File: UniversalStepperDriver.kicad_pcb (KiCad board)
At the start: 2 copper layers, 65 x 56.5 mm, 84 parts, among them P1 USB_OTG, P11 CONN_01X04, P12 CONN_01X02, P13 CONN_28BYJ-48, P14 CONN_28BYJ-48, P15 CONN_28BYJ-48, P17 CONN_01X04, P2 CONN_01X02, P3 CONN_01X02, P4 CONN_01X03, P5 Universal_Serial_Connector, P6 CONN_01X06, P7 RPI_header, P8 CONN_01X03, P9 CONN_01X04, SW1 SW_PUSH, SW2 SW_PUSH, SW3 SW_PUSH, U1 STM32F411RE, U2 INA169, U3 MPQ4420, U4 ULN2003V, U5 ULN2003V, Y1 CRYSTAL_SMD

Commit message: all connected
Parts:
- JP1: moved to B.Cu
- SW1: footprint Buttons_Switches_SMD:SW_SPST_SKQG -> KSEK43J_LFS_TACTILE_SWITCH:KSEK43J_LFS_TACTILE_SWITCH
- SW2, SW3: footprint Buttons_Switches_SMD:SW_SPST_EVQP7C -> Buttons_Switches_ThroughHole:SW_Tactile_SPST_Angled
- Y1: value CRYSTAL_SMD -> CRYSTAL_SMD_16MHz
- moved JP1 28.3 mm to (113.7, 87.8), turned to 0 degrees
- moved R12 8.06 mm to (125.3, 111.4)
- moved D2 8.06 mm to (123.4, 111.3)
- moved R27 7.57 mm to (106.4, 109.2), turned to 180 degrees
- moved C16 7.44 mm to (113.5, 107.4)
- moved R16 6.22 mm to (115.0, 115.9), turned to 90 degrees
- moved R10 5.67 mm to (118.5, 120.2), turned to 0 degrees
- moved C13 5.64 mm to (112.3, 114.7)
- moved D1 4.74 mm to (129.8, 111.4)
- moved R11 4.65 mm to (131.7, 111.4)
- moved R25 4.38 mm to (109.7, 109.2), turned to 180 degrees
- moved P9 3.92 mm to (114.0, 97.1)
- moved JP6 3.62 mm to (109.8, 81.1), turned to 180 degrees
- moved P11 3.61 mm to (110.4, 97.1)
- moved R15 3.57 mm to (112.5, 120.0), turned to 270 degrees
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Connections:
- C12 pad 1: /X_MAX -> /X_LIMIT
- C13 pad 1: /Y_MAX -> /Y_LIMIT
- R13 pad 2: /X_MAX -> /X_LIMIT
- R14 pad 2: /Y_MAX -> /Y_LIMIT
- SW2 pad 1: /X_MAX -> /X_LIMIT
- SW3 pad 1: /Y_MAX -> /Y_LIMIT
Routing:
- net GND: track 46.8 -> 452.0 mm, vias 5 -> 23
- net +3V3: track 10.3 -> 235.6 mm, vias 0 -> 14
- net /X_LIMIT: track 23.1 -> 73.6 mm, vias 0 -> 1
- net /SDA_I2C: track 0.00 -> 44.8 mm, vias 0 -> 1
- net /RxD: track 24.6 -> 65.4 mm, vias 1 -> 4
- net /SCL_I2C: track 0.00 -> 40.6 mm, vias 0 -> 1
- net /Y_LIMIT: track 31.2 -> 68.8 mm
- net /RST: track 7.25 -> 43.5 mm, vias 0 -> 2
- net /GPI: track 0.00 -> 35.1 mm
- net /SERVO_PWM: track 0.00 -> 33.7 mm, vias 0 -> 1
- net /SCK_SPI: track 0.00 -> 32.5 mm, vias 0 -> 1
- net /Y_ENC_A: track 0.00 -> 31.4 mm, vias 0 -> 1
- net /X_ENC_B: track 0.00 -> 29.6 mm, vias 0 -> 1
- net /Y_ENC_B: track 0.00 -> 27.8 mm, vias 0 -> 1
- net /X_ENC_A: track 0.00 -> 25.7 mm, vias 0 -> 1
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
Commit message: rev0.1 board done
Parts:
- added G***: LOGO, .pretty:LOGO_irnas1, B.Cu at (138.0, 100.2)
- moved P8 0.98 mm to (148.7, 111.1)
- moved C2 0.60 mm to (118.2, 101.4)
- moved C4 0.60 mm to (119.7, 101.4)
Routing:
- net +3V3: track 235.6 -> 278.9 mm
- net VAA: track 107.7 -> 117.4 mm
- net VCC: track 30.9 -> 34.9 mm
- net /USB_D_N: track 43.3 -> 44.5 mm
- net /STPEN: track 29.7 -> 28.9 mm
- net /SERVO_PWM: track 33.7 -> 32.9 mm
- net /M1_STEP: track 31.3 -> 30.8 mm
- net GND: track 452.0 -> 452.5 mm
- added copper zone on F.Cu, net +3V3
- added copper zone on B.Cu, net GND
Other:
- board text added: "+"
- board text added: "-"
- board text added: "CERN OHL"
- board text added: "F"
- board text added: "USB"
- board text added: "Universal Stepper Driver"
- board text added: "VCC"
- board text added: "V_3"
- board text added: "WWW.IRNAS.EU"
- board text added: "X"
- board text added: "Y"
- board text added: "s"
- board text removed: "CERN OHL V1.2"
- board text removed: "Julien M."

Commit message: add gerber and BOM
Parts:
- C10: footprint Capacitors_SMD:C_0603 -> Capacitors_SMD:C_1206
- moved C10 0.64 mm to (161.6, 74.2)
- turned JP7 to 90 degrees
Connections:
- Y1 pad 2: Net-(Y1-Pad2) -> GND
- Y1 pad 4: (no net) -> GND
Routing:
- net GND: track 452.5 -> 460.8 mm
- net 5V_RPi: track 54.9 -> 50.7 mm
- net VAA: track 117.4 -> 116.5 mm
- net /C_X_4: track 29.2 -> 29.8 mm

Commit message: P5 footprint fix
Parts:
- P5: footprint .pretty:micromatch -> micromatch
- moved JP3 3.80 mm to (116.1, 83.6)
- moved JP1 2.95 mm to (116.1, 86.1)
- moved JP6 1.06 mm to (108.8, 81.2)
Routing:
- net /MISO_SPI: track 36.6 -> 32.5 mm
- net /TxD: track 49.5 -> 46.9 mm
- net Net-(JP1-Pad1): track 5.66 -> 3.81 mm
- net /SCL_I2C: track 40.6 -> 39.0 mm
- net Net-(JP3-Pad1): track 5.44 -> 3.86 mm
- net /CS_SPI: track 24.3 -> 25.8 mm
- net Net-(JP5-Pad1): track 6.83 -> 7.97 mm
- net /RxD: track 65.4 -> 66.3 mm
- net /F_LIMIT: track 50.0 -> 50.7 mm
- net GND: track 460.8 -> 461.4 mm, vias 23 -> 22

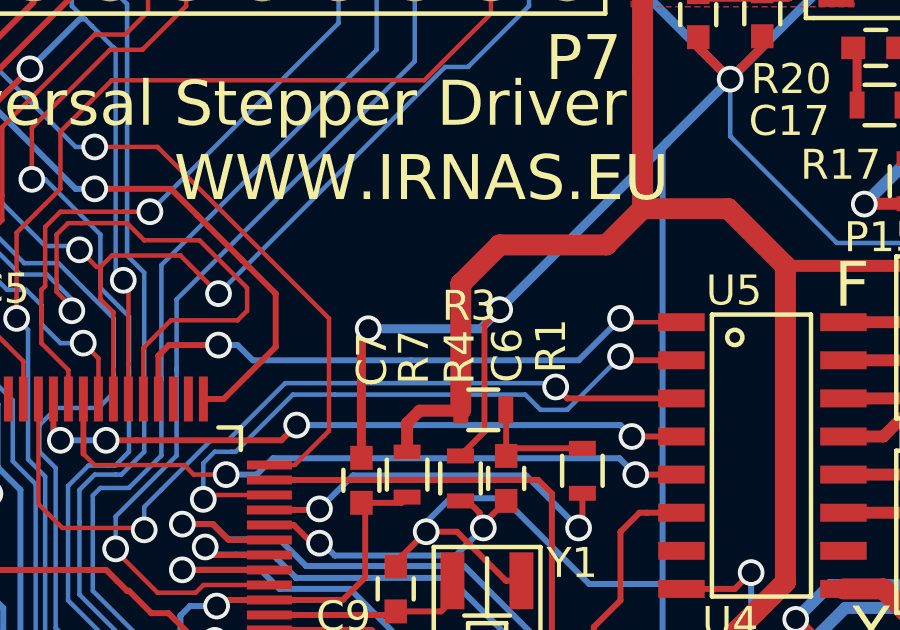
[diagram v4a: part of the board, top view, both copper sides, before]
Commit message: PWR LED add Fixes #3
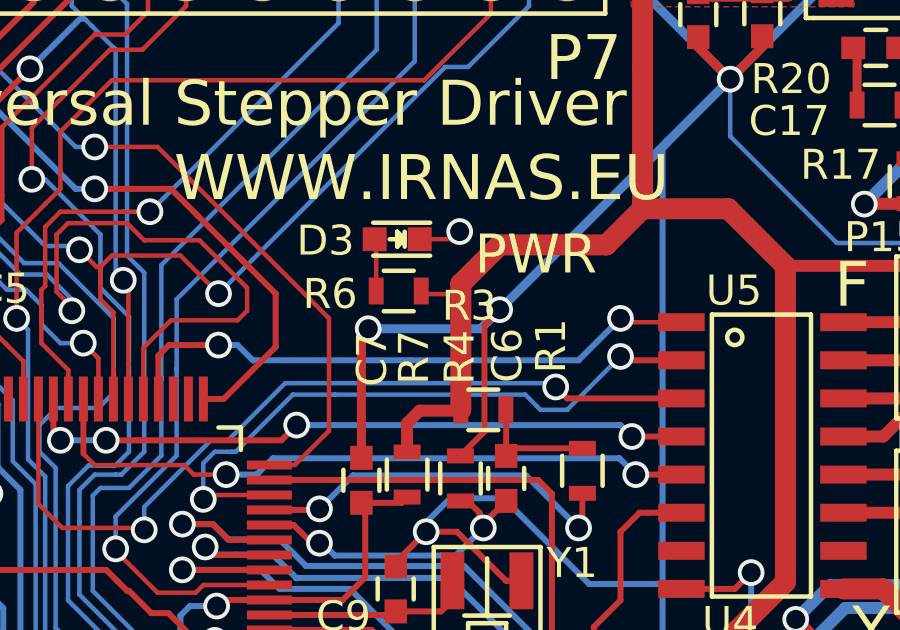
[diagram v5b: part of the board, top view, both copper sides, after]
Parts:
- added D3: LED_GREEN, LEDs:LED_0603, F.Cu at (138.1, 84.8)
- added R6: 1k, Resistors_SMD:R_0603, F.Cu at (138.2, 86.6)
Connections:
- Y1 pad 2: GND -> Net-(Y1-Pad2)
- Y1 pad 4: GND -> (no net)
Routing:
- net Net-(D3-Pad2): track 0.00 -> 1.75 mm
- net +3V3: track 278.9 -> 280.3 mm
- net GND: track 461.4 -> 462.4 mm, vias 22 -> 23
- net Net-(Y1-Pad2): track 0.00 -> 0.51 mm
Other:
- board text added: "PWR"
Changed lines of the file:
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@@
 (kicad_pcb (version 4) (host pcbnew 4.0.2-stable)
   (general
-    (links 224)
+    (links 225)
     (no_connects 0)
-    (area 100.838261 67.828761 177.679167 136.400001)
+    (area 104.869999 71.019999 169.970001 127.620001)
     (thickness 1.6)
-    (drawings 35)
-    (tracks 1645)
+    (drawings 36)
+    (tracks 1653)
     (zones 0)
-    (modules 85)
-    (nets 108)
+    (modules 87)
+    (nets 110)
   )
   (page A4)
@@
   (net 106 "Net-(U5-Pad10)")
   (net 107 "Net-(U1-Pad30)")
+  (net 108 "Net-(Y1-Pad2)")
+  (net 109 "Net-(D3-Pad2)")
   (net_class Default "This is the default net class."
     (clearance 0.15)
@@
     (add_net "Net-(D1-Pad2)")
     (add_net "Net-(D2-Pad2)")
+    (add_net "Net-(D3-Pad2)")
     (add_net "Net-(F1-Pad1)")
     (add_net "Net-(JP1-Pad1)")
@@
     (add_net "Net-(U5-Pad10)")
     (add_net "Net-(U5-Pad7)")
+    (add_net "Net-(Y1-Pad2)")
     (add_net VAA)
     (add_net VCC)
@@
       (net 9 /OSCIN_8M))
     (pad 2 smd rect (at 3.7 0 90) (size 1.9 0.8) (layers F.Cu F.Paste F.Mask)
-      (net 1 GND))
+      (net 108 "Net-(Y1-Pad2)"))
     (pad 3 smd rect (at 3.7 -2.3 90) (size 1.9 0.8) (layers F.Cu F.Paste F.Mask)
       (net 10 /OSCOUT_8M))
-    (pad 4 smd rect (at 0 -2.3 90) (size 1.9 0.8) (layers F.Cu F.Paste F.Mask)
-      (net 1 GND))
+    (pad 4 smd rect (at 0 -2.3 90) (size 1.9 0.8) (layers F.Cu F.Paste F.Mask))
   )
   (module .pretty:bridgeJumper (layer B.Cu)
@@
     )
   )
+  (module LEDs:LED_0603 (layer F.Cu)
+    (at 138.1252 84.836 180)
+    (descr "LED 0603 smd package")
+    (tags "LED led 0603 SMD smd SMT smt smdled SMDLED smtled SMTLED")
+    (attr smd)
+    (fp_text reference D3 (at 2.3876 -0.0508 180) (layer F.SilkS)
+      (effects (font (size 1 1) (thickness 0.15)))
+    )
+    (fp_text value LED_GREEN (at 0 1.5 180) (layer F.Fab)
+      (effects (font (size 1 1) (thickness 0.15)))
+    )
+    (fp_line (start -1.1 0.55) (end 0.8 0.55) (layer F.SilkS) (width 0.15))
+    (fp_line (start -1.1 -0.55) (end 0.8 -0.55) (layer F.SilkS) (width 0.15))
+    (fp_line (start -0.2 0) (end 0.25 0) (layer F.SilkS) (width 0.15))
+    (fp_line (start -0.25 -0.25) (end -0.25 0.25) (layer F.SilkS) (width 0.15))
+    (fp_line (start -0.25 0) (end 0 -0.25) (layer F.SilkS) (width 0.15))
+    (fp_line (start 0 -0.25) (end 0 0.25) (layer F.SilkS) (width 0.15))
+    (fp_line (start 0 0.25) (end -0.25 0) (layer F.SilkS) (width 0.15))
+    (fp_line (start 1.4 -0.75) (end 1.4 0.75) (layer F.CrtYd) (width 0.05))
+    (fp_line (start 1.4 0.75) (end -1.4 0.75) (layer F.CrtYd) (width 0.05))
+    (fp_line (start -1.4 0.75) (end -1.4 -0.75) (layer F.CrtYd) (width 0.05))
+    (fp_line (start -1.4 -0.75) (end 1.4 -0.75) (layer F.CrtYd) (width 0.05))
+    (pad 2 smd rect (at 0.7493 0) (size 0.79756 0.79756) (layers F.Cu F.Paste F.Mask)
+      (net 109 "Net-(D3-Pad2)"))
+    (pad 1 smd rect (at -0.7493 0) (size 0.79756 0.79756) (layers F.Cu F.Paste F.Mask)
+      (net 1 GND))
+    (model LEDs.3dshapes/LED_0603.wrl
+      (at (xyz 0 0 0))
+      (scale (xyz 1 1 1))
+      (rotate (xyz 0 0 180))
+    )
+  )
+  (module Resistors_SMD:R_0603 (layer F.Cu)
+    (at 138.176 86.5632)
+    (descr "Resistor SMD 0603, reflow soldering, Vishay (see dcrcw.pdf)")
+    (tags "resistor 0603")
+    (attr smd)
+    (fp_text reference R6 (at -2.286 0.1016) (layer F.SilkS)
+      (effects (font (size 1 1) (thickness 0.15)))
+    )
+    (fp_text value 1k (at 0 1.9) (layer F.Fab)
+      (effects (font (size 1 1) (thickness 0.15)))
+    )
+    (fp_line (start -1.3 -0.8) (end 1.3 -0.8) (layer F.CrtYd) (width 0.05))
+    (fp_line (start -1.3 0.8) (end 1.3 0.8) (layer F.CrtYd) (width 0.05))
+    (fp_line (start -1.3 -0.8) (end -1.3 0.8) (layer F.CrtYd) (width 0.05))
+    (fp_line (start 1.3 -0.8) (end 1.3 0.8) (layer F.CrtYd) (width 0.05))
+    (fp_line (start 0.5 0.675) (end -0.5 0.675) (layer F.SilkS) (width 0.15))
+    (fp_line (start -0.5 -0.675) (end 0.5 -0.675) (layer F.SilkS) (width 0.15))
+    (pad 1 smd rect (at -0.75 0) (size 0.5 0.9) (layers F.Cu F.Paste F.Mask)
+      (net 109 "Net-(D3-Pad2)"))
+    (pad 2 smd rect (at 0.75 0) (size 0.5 0.9) (layers F.Cu F.Paste F.Mask)
+      (net 2 +3V3))
+    (model Resistors_SMD.3dshapes/R_0603.wrl
+      (at (xyz 0 0 0))
+      (scale (xyz 1 1 1))
+      (rotate (xyz 0 0 0))
+    )
+  )
+  (gr_text PWR (at 142.748 85.344) (layer F.SilkS)
+    (effects (font (size 1.3 1.3) (thickness 0.3)))
+  )
   (gr_text V_3 (at 121.412 82.7405) (layer F.SilkS)
     (effects (font (size 1.5 1.5) (thickness 0.3)))
@@
   (gr_arc (start 166.92 74.07) (end 166.92 71.07) (angle 90) (layer Edge.Cuts) (width 0.1))
   (gr_arc (start 107.92 124.57) (end 107.92 127.57) (angle 90) (layer Edge.Cuts) (width 0.1))
+  (segment (start 138.8745 84.836) (end 139.954 84.836) (width 0.15) (layer F.Cu) (net 1) (status 400000))
+  (via (at 140.208 84.582) (size 0.889) (drill 0.635) (layers F.Cu B.Cu) (net 1))
+  (segment (start 139.954 84.836) (end 140.208 84.582) (width 0.15) (layer F.Cu) (net 1))
   (segment (start 114.046 84.836) (end 118.5672 84.836) (width 0.2) (layer B.Cu) (net 1))
   (segment (start 119.4816 85.7504) (end 120.5992 85.7504) (width 0.2) (layer B.Cu) (net 1))
@@
   (segment (start 160.8083 73.5307) (end 161.6075 72.7315) (width 0.7) (layer F.Cu) (net 1))
   (segment (start 139.091 94.588) (end 140.1175 94.588) (width 0.2) (layer F.Cu) (net 1))
-  (segment (start 141.7515 96.222) (end 142.266 96.222) (width 0.2) (layer F.Cu) (net 1))
   (segment (start 140.1175 94.588) (end 141.7515 96.222) (width 0.2) (layer F.Cu) (net 1))
   (segment (start 139.966 99.922) (end 138.317 99.922) (width 0.2) (layer F.Cu) (net 1))
@@
   (segment (start 146.452 125.782) (end 156.966 125.782) (width 2) (layer F.Cu) (net 1))
   (segment (start 156.966 125.782) (end 159.966 122.782) (width 2) (layer F.Cu) (net 1))
+  (segment (start 140.246 86.6648) (end 139.0276 86.6648) (width 0.15) (layer F.Cu) (net 2) (status 800000))
+  (segment (start 139.0276 86.6648) (end 138.926 86.5632) (width 0.15) (layer F.Cu) (net 2) (status C00000))
   (segment (start 151.003 106.4895) (end 153.2255 108.712) (width 0.7) (layer B.Cu) (net 2))
   (segment (start 153.2255 108.712) (end 159.131 108.712) (width 0.7) (layer B.Cu) (net 2))
@@
   (segment (start 146.304 83.82) (end 149.1615 83.82) (width 0.7) (layer F.Cu) (net 2))
   (segment (start 149.1615 83.82) (end 151.0665 85.725) (width 0.7) (layer F.Cu) (net 2))
-  (segment (start 140.246 86.322) (end 140.246 90.524) (width 0.7) (layer F.Cu) (net 2))
+  (segment (start 140.246 86.322) (end 140.246 86.6648) (width 0.7) (layer F.Cu) (net 2))
+  (segment (start 140.246 86.6648) (end 140.246 90.524) (width 0.7) (layer F.Cu) (net 2))
   (segment (start 146.304 79.1845) (end 146.304 83.82) (width 0.7) (layer F.Cu) (net 2))
   (segment (start 141.5415 85.0265) (end 140.246 86.322) (width 0.7) (layer F.Cu) (net 2))
@@
   (segment (start 111.913 74.649) (end 111.913 72.49) (width 0.4) (layer B.Cu) (net 100))
   (segment (start 112.167 74.903) (end 111.913 74.649) (width 0.4) (layer B.Cu) (net 100))
+  (segment (start 141.7515 96.222) (end 142.266 96.222) (width 0.2) (layer F.Cu) (net 108))
+  (segment (start 137.426 86.5632) (end 137.426 84.8861) (width 0.15) (layer F.Cu) (net 109) (status C00000))
+  (segment (start 137.426 84.8861) (end 137.3759 84.836) (width 0.15) (layer F.Cu) (net 109) (status C00000))
   (zone (net 0) (net_name "") (layer B.Cu) (hatch edge 0.508)
     (connect_pads (clearance 0.15))

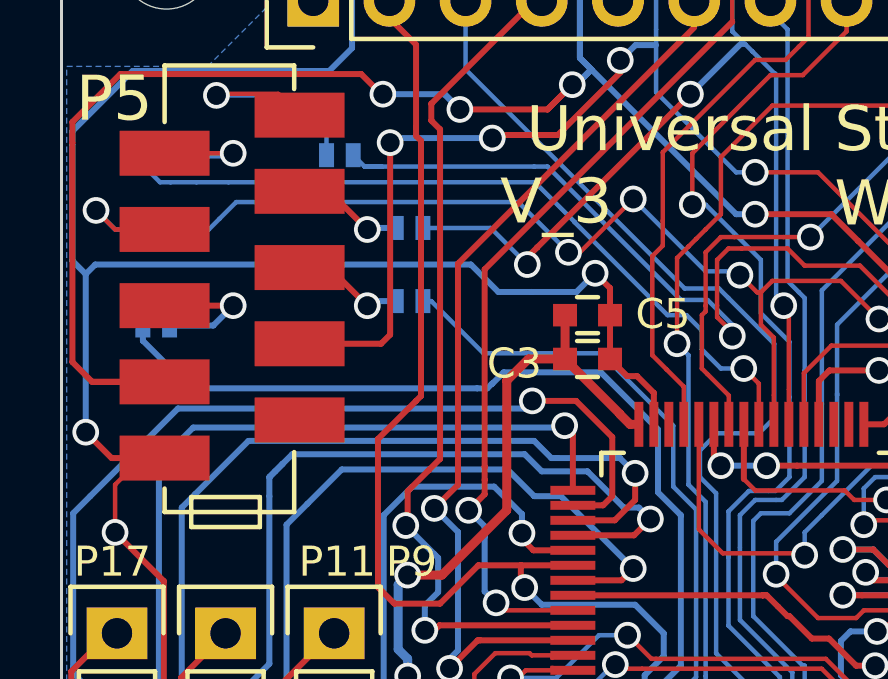
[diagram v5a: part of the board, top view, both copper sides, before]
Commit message: add VCAP1 4.7u to PIN30(PB11) Fixes #2
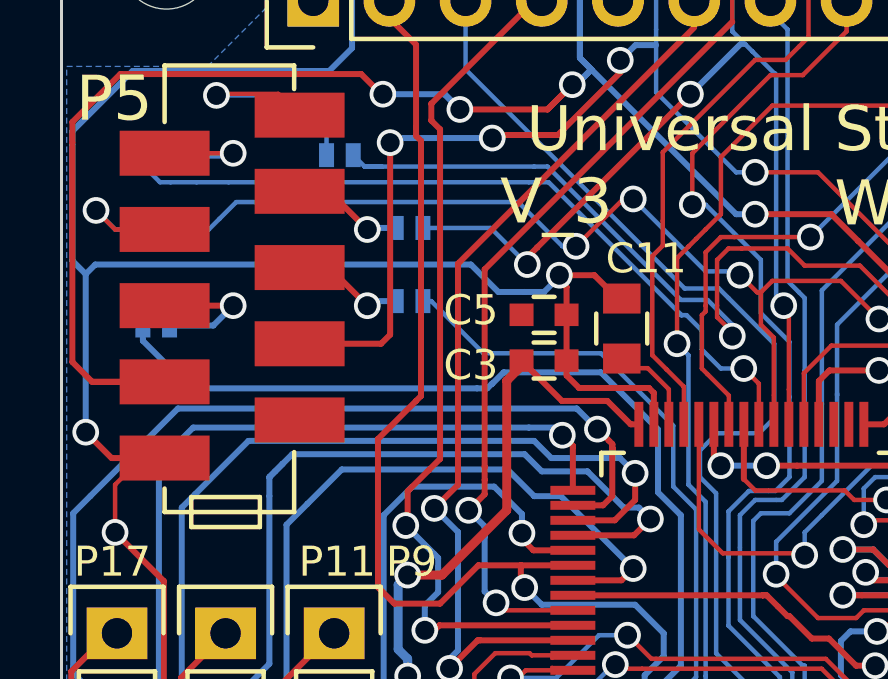
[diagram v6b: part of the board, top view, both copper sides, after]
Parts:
- added C11: 4.7uF, Capacitors_SMD:C_0805, F.Cu at (123.6, 87.0)
- moved C3 1.45 mm to (121.0, 88.0)
- moved C5 1.45 mm to (121.0, 86.5)
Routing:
- net Net-(C11-Pad1): track 0.00 -> 2.87 mm
- net GND: track 462.4 -> 465.2 mm
- net +3V3: track 280.3 -> 279.0 mm
